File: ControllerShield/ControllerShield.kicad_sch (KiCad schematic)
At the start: 27 parts, among them J1 Power, J2 Digital/PWM, J3 Analog, J4 Digital/PWM, J5 Conn_02x05_Odd_Even, SW1 Small Switch TH, SW2 Small Switch TH, U1 COM-09032, U2 LIS3DHTR, U3 TLV75533PDBV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

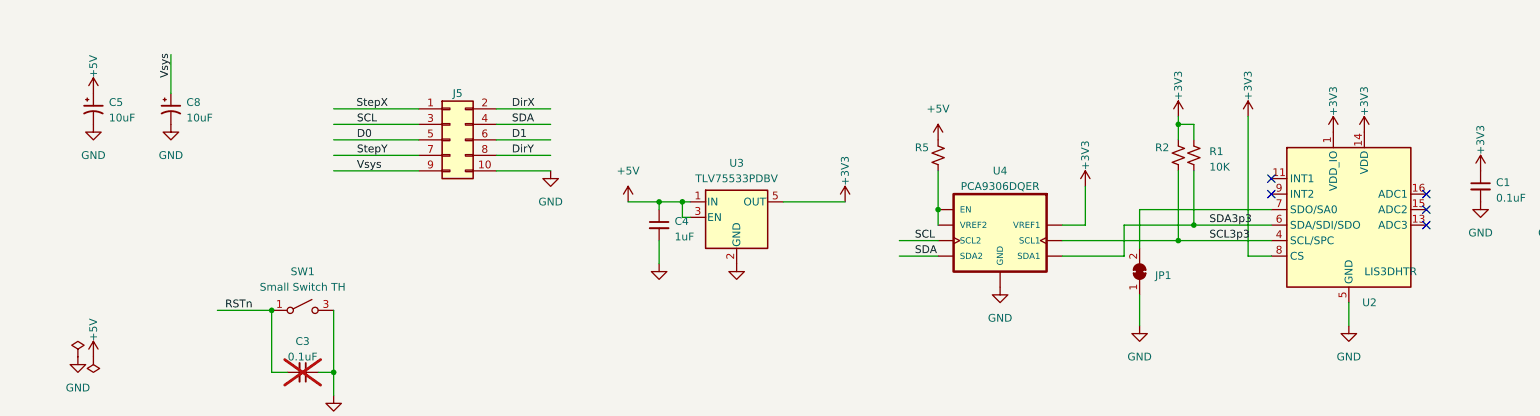
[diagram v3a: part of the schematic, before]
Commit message: bom changes
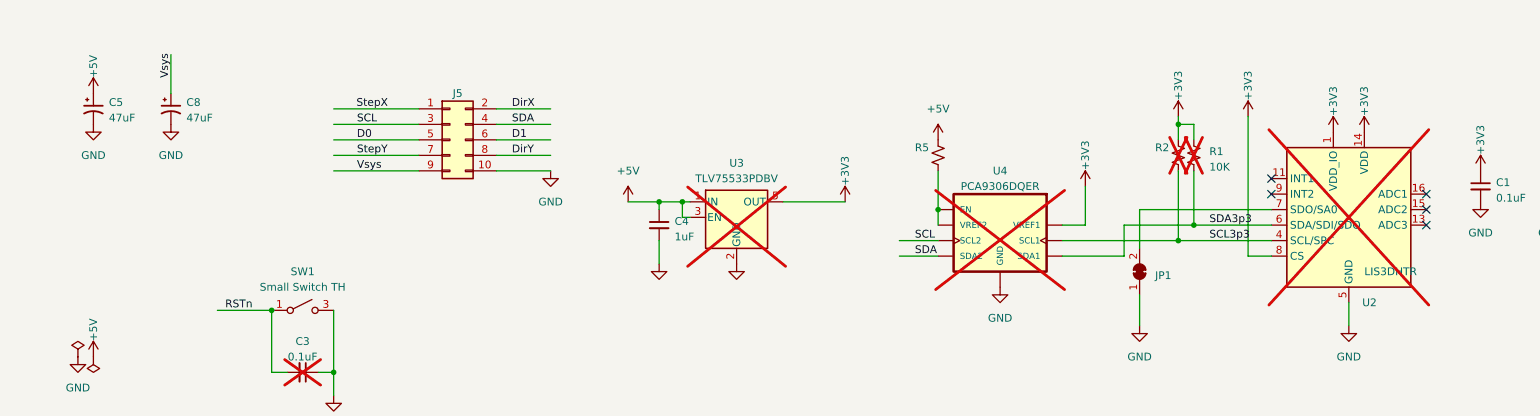
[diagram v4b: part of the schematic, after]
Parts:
- C1, C3, C6, C7: Vendor (none) -> 1276-1000-1-ND
- C2: Vendor (none) -> 490-GRM188R61E106KA73JCT-ND
- C4: Digikey (none) -> CL10A105KL8NNNC; Vendor (none) -> CL10A105KL8NNNC
- C5, C8: value 10uF -> 47uF; Digikey (none) -> 10-ECE-A1EKA470ICT-ND; Vendor (none) -> 10-ECE-A1EKA470ICT-ND
- D1: Vendor (none) -> 1125-1188-ND; now left out of the parts list
- D2: Vendor (none) -> 1125-1184-ND; now left out of the parts list
- J1, J4: Digikey (none) -> 2057-PH1-08-UA-ND; Vendor (none) -> 2057-PH1-08-UA-ND
- J2: Digikey (none) -> 2057-PH1-10-UA-ND; Vendor (none) -> 2057-PH1-10-UA-ND
- J3: Vendor (none) -> 2057-PH1-06-UA-ND; digikey (none) -> 2057-PH1-06-UA-ND
- J5: Vendor (none) -> 732-2094-ND
- R1, R2: Vendor (none) -> RMCF0603FT10K0CT-ND; now not fitted; now left out of the parts list
- R3, R4: Vendor (none) -> RMCF0603FT1K00CT-ND
- R5: Vendor (none) -> RMCF0603FT10K0CT-ND
- SW1, SW2: Vendor (none) -> 450-1650-ND
- U1: Digikey (none) -> 1568-1526-ND; Vendor (none) -> 1568-1526-ND
- U2: Vendor (none) -> 497-10613-1-ND; now not fitted; now left out of the parts list
- U3: Vendor (none) -> 296-50411-1-ND; now not fitted; now left out of the parts list
- U4: DigiKey 296-18509-2-ND -> 296-18509-1-ND; Vendor 296-18509-2-ND -> 296-18509-1-ND; now not fitted; now left out of the parts list
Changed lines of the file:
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@@
       (effects (font (size 1.27 1.27)))
+    )
+    (property "Digikey" "2057-PH1-08-UA-ND" (at 39.37 39.37 0)
+      (effects (font (size 1.27 1.27)) hide)
+    )
+    (property "Vendor" "2057-PH1-08-UA-ND" (at 39.37 39.37 0)
+      (effects (font (size 1.27 1.27)) hide)
     )
     (pin "1")
@@
     (property "Datasheet" "~" (at 57.15 36.83 0)
       (effects (font (size 1.27 1.27)))
+    )
+    (property "Digikey" "2057-PH1-10-UA-ND" (at 57.15 36.83 0)
+      (effects (font (size 1.27 1.27)) hide)
+    )
+    (property "Vendor" "2057-PH1-10-UA-ND" (at 57.15 36.83 0)
+      (effects (font (size 1.27 1.27)) hide)
     )
     (pin "1")
@@
       (effects (font (size 1.27 1.27)) hide)
     )
+    (property "digikey" "2057-PH1-06-UA-ND" (at 39.37 64.77 0)
+      (effects (font (size 1.27 1.27)) hide)
+    )
+    (property "Vendor" "2057-PH1-06-UA-ND" (at 39.37 64.77 0)
+      (effects (font (size 1.27 1.27)) hide)
+    )
     (pin "1")
     (pin "2")
@@
     (property "Datasheet" "~" (at 57.15 67.31 0)
       (effects (font (size 1.27 1.27)))
+    )
+    (property "Digikey" "2057-PH1-08-UA-ND" (at 57.15 67.31 0)
+      (effects (font (size 1.27 1.27)) hide)
+    )
+    (property "Vendor" "2057-PH1-08-UA-ND" (at 57.15 67.31 0)
+      (effects (font (size 1.27 1.27)) hide)
     )
     (pin "1")
@@
   )
   (symbol (lib_id "Device:R_Small_US") (at 212.09 109.22 0) (unit 1)
-    (in_bom yes) (on_board yes) (dnp no) (fields_autoplaced)
+    (in_bom no) (on_board yes) (dnp yes) (fields_autoplaced)
     (property "Reference" "R1" (at 214.63 108.585 0)
       (effects (font (size 1.27 1.27)) (justify left))
@@
     )
     (property "Digikey" "RMCF0603FT10K0CT-ND" (at 212.09 109.22 0)
+      (effects (font (size 1.27 1.27)) hide)
+    )
+    (property "Vendor" "RMCF0603FT10K0CT-ND" (at 212.09 109.22 0)
       (effects (font (size 1.27 1.27)) hide)
     )
@@
     )
     (property "Datasheet" "" (at 193.04 49.53 0)
+      (effects (font (size 1.27 1.27)) hide)
+    )
+    (property "Digikey" "1568-1526-ND" (at 193.04 49.53 0)
+      (effects (font (size 1.27 1.27)) hide)
+    )
+    (property "Vendor" "1568-1526-ND" (at 193.04 49.53 0)
       (effects (font (size 1.27 1.27)) hide)
     )
@@
       (effects (font (size 1.27 1.27)) hide)
     )
+    (property "Vendor" "450-1650-ND" (at 66.04 134.62 0)
+      (effects (font (size 1.27 1.27)) hide)
+    )
     (pin "1")
     (pin "2")
@@
     )
     (property "Digikey" "RMCF0603FT1K00CT-ND" (at 116.84 45.72 0)
+      (effects (font (size 1.27 1.27)) hide)
+    )
+    (property "Vendor" "RMCF0603FT1K00CT-ND" (at 116.84 45.72 0)
       (effects (font (size 1.27 1.27)) hide)
     )
@@
       (effects (font (size 1.27 1.27)) hide)
     )
+    (property "Vendor" "1276-1000-1-ND" (at 66.04 144.78 0)
+      (effects (font (size 1.27 1.27)) hide)
+    )
     (pin "1")
     (pin "2")
@@
     )
     (property "Digikey" "732-2094-ND" (at 90.17 106.68 0)
+      (effects (font (size 1.27 1.27)) hide)
+    )
+    (property "Vendor" "732-2094-ND" (at 90.17 106.68 0)
       (effects (font (size 1.27 1.27)) hide)
     )
@@
       (effects (font (size 1.27 1.27)) (justify left))
     )
-    (property "Value" "10uF" (at 34.29 103.0732 0)
+    (property "Value" "47uF" (at 34.29 103.0732 0)
       (effects (font (size 1.27 1.27)) (justify left))
     )
@@
     )
     (property "Datasheet" "~" (at 31.75 101.6 0)
+      (effects (font (size 1.27 1.27)) hide)
+    )
+    (property "Digikey" "10-ECE-A1EKA470ICT-ND" (at 31.75 101.6 0)
+      (effects (font (size 1.27 1.27)) hide)
+    )
+    (property "Vendor" "10-ECE-A1EKA470ICT-ND" (at 31.75 101.6 0)
       (effects (font (size 1.27 1.27)) hide)
     )
@@
   )
   (symbol (lib_id "Device:LED") (at 116.84 54.61 90) (unit 1)
-    (in_bom yes) (on_board yes) (dnp no)
+    (in_bom no) (on_board yes) (dnp no)
     (property "Reference" "D2" (at 119.38 53.34 90)
       (effects (font (size 1.27 1.27)) (justify right))
@@
       (effects (font (size 1.27 1.27)) hide)
     )
+    (property "Vendor" "1125-1184-ND" (at 116.84 54.61 0)
+      (effects (font (size 1.27 1.27)) hide)
+    )
     (pin "1")
     (pin "2")
@@
   )
   (symbol (lib_id "Regulator_Linear:TLV75533PDBV") (at 137.16 119.38 0) (unit 1)
-    (in_bom yes) (on_board yes) (dnp no) (fields_autoplaced)
+    (in_bom no) (on_board yes) (dnp yes) (fields_autoplaced)
     (property "Reference" "U3" (at 137.16 110.49 0)
       (effects (font (size 1.27 1.27)))
@@
     )
     (property "Digikey" "296-50411-1-ND" (at 137.16 119.38 0)
+      (effects (font (size 1.27 1.27)) hide)
+    )
+    (property "Vendor" "296-50411-1-ND" (at 137.16 119.38 0)
       (effects (font (size 1.27 1.27)) hide)
     )
@@
   )
   (symbol (lib_id "Device:R_Small_US") (at 209.55 109.22 0) (unit 1)
-    (in_bom yes) (on_board yes) (dnp no)
+    (in_bom no) (on_board yes) (dnp yes)
     (property "Reference" "R2" (at 205.74 107.95 0)
       (effects (font (size 1.27 1.27)) (justify left))
@@
       (effects (font (size 1.27 1.27)) hide)
     )
+    (property "Vendor" "RMCF0603FT10K0CT-ND" (at 209.55 109.22 0)
+      (effects (font (size 1.27 1.27)) hide)
+    )
     (pin "1")
     (pin "2")
@@
     )
     (property "Digikey" "450-1650-ND" (at 66.04 166.37 0)
+      (effects (font (size 1.27 1.27)) hide)
+    )
+    (property "Vendor" "450-1650-ND" (at 66.04 166.37 0)
       (effects (font (size 1.27 1.27)) hide)
     )
@@
       (effects (font (size 1.27 1.27)) hide)
     )
+    (property "Vendor" "1276-1000-1-ND" (at 168.91 63.5 0)
+      (effects (font (size 1.27 1.27)) hide)
+    )
     (pin "1")
     (pin "2")
@@
   )
   (symbol (lib_id "StockedComponents:PCA9306DQER") (at 175.26 130.81 0) (mirror y) (unit 1)
-    (in_bom yes) (on_board yes) (dnp no) (fields_autoplaced)
+    (in_bom no) (on_board yes) (dnp yes) (fields_autoplaced)
     (property "Reference" "U4" (at 180.34 111.76 0)
       (effects (font (size 1.27 1.27)))
@@
       (effects (font (size 1.27 1.27)) hide)
     )
-    (property "DigiKey" "296-18509-2-ND" (at 175.26 130.81 0)
-      (effects (font (size 1.27 1.27)) hide)
-    )
-    (property "Vendor" "296-18509-2-ND" (at 175.26 130.81 0)
+    (property "DigiKey" "296-18509-1-ND" (at 175.26 130.81 0)
+      (effects (font (size 1.27 1.27)) hide)
+    )
+    (property "Vendor" "296-18509-1-ND" (at 175.26 130.81 0)
       (effects (font (size 1.27 1.27)) hide)
     )
@@
   )
   (symbol (lib_id "Sensor_Motion:LIS3DH") (at 237.49 118.11 0) (unit 1)
-    (in_bom yes) (on_board yes) (dnp no)
+    (in_bom no) (on_board yes) (dnp yes)
     (property "Reference" "U2" (at 239.6841 133.35 0)
       (effects (font (size 1.27 1.27)) (justify left))
@@
     )
     (property "Digikey" "497-10613-1-ND" (at 237.49 118.11 0)
+      (effects (font (size 1.27 1.27)) hide)
+    )
+    (property "Vendor" "497-10613-1-ND" (at 237.49 118.11 0)
       (effects (font (size 1.27 1.27)) hide)
     )
@@
       (effects (font (size 1.27 1.27)) hide)
     )
+    (property "Vendor" "1276-1000-1-ND" (at 66.04 176.53 0)
+      (effects (font (size 1.27 1.27)) hide)
+    )
     (pin "1")
     (pin "2")
@@
   )
   (symbol (lib_id "Device:LED") (at 109.22 54.61 90) (unit 1)
-    (in_bom yes) (on_board yes) (dnp no)
+    (in_bom no) (on_board yes) (dnp no)
     (property "Reference" "D1" (at 104.14 53.34 90)
       (effects (font (size 1.27 1.27)) (justify right))
@@
       (effects (font (size 1.27 1.27)) hide)
     )
+    (property "Vendor" "1125-1188-ND" (at 109.22 54.61 0)
+      (effects (font (size 1.27 1.27)) hide)
+    )
     (pin "1")
     (pin "2")
@@
     )
     (property "Digikey" "490-GRM188R61E106KA73JCT-ND" (at 270.51 114.3 0)
+      (effects (font (size 1.27 1.27)) hide)
+    )
+    (property "Vendor" "490-GRM188R61E106KA73JCT-ND" (at 270.51 114.3 0)
       (effects (font (size 1.27 1.27)) hide)
     )
@@
       (effects (font (size 1.27 1.27)) hide)
     )
+    (property "Vendor" "RMCF0603FT10K0CT-ND" (at 170.18 109.22 0)
+      (effects (font (size 1.27 1.27)) hide)
+    )
     (pin "1")
     (pin "2")
@@
       (effects (font (size 1.27 1.27)) (justify left))
     )
-    (property "Value" "10uF" (at 46.99 103.0732 0)
+    (property "Value" "47uF" (at 46.99 103.0732 0)
       (effects (font (size 1.27 1.27)) (justify left))
     )
@@
       (effects (font (size 1.27 1.27)) hide)
     )
+    (property "Digikey" "10-ECE-A1EKA470ICT-ND" (at 44.45 101.6 0)
+      (effects (font (size 1.27 1.27)) hide)
+    )
+    (property "Vendor" "10-ECE-A1EKA470ICT-ND" (at 44.45 101.6 0)
+      (effects (font (size 1.27 1.27)) hide)
+    )
     (pin "1")
     (pin "2")
@@
       (effects (font (size 1.27 1.27)) hide)
     )
+    (property "Digikey" "CL10A105KL8NNNC" (at 124.46 120.65 0)
+      (effects (font (size 1.27 1.27)) hide)
+    )
+    (property "Vendor" "CL10A105KL8NNNC" (at 124.46 120.65 0)
+      (effects (font (size 1.27 1.27)) hide)
+    )
     (pin "1")
     (pin "2")
@@
       (effects (font (size 1.27 1.27)) hide)
     )
+    (property "Vendor" "1276-1000-1-ND" (at 259.08 114.3 0)
+      (effects (font (size 1.27 1.27)) hide)
+    )
     (pin "1")
     (pin "2")
@@
       (effects (font (size 1.27 1.27)) hide)
     )
+    (property "Vendor" "RMCF0603FT1K00CT-ND" (at 109.22 45.72 0)
+      (effects (font (size 1.27 1.27)) hide)
+    )
